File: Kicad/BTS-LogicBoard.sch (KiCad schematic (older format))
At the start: 39 parts, among them J1 Conn_01x06, J2 Conn_01x04, J3 Conn_01x02, SW1 SW_DPDT_x2, SW2 SW_DPDT_x2, U1 NCS2252SN2T1G, U2 NE555D, U3 74HC1GU04, U4 TLP291, U5 74HC1GU04, U6 NCS2252SN2T1G

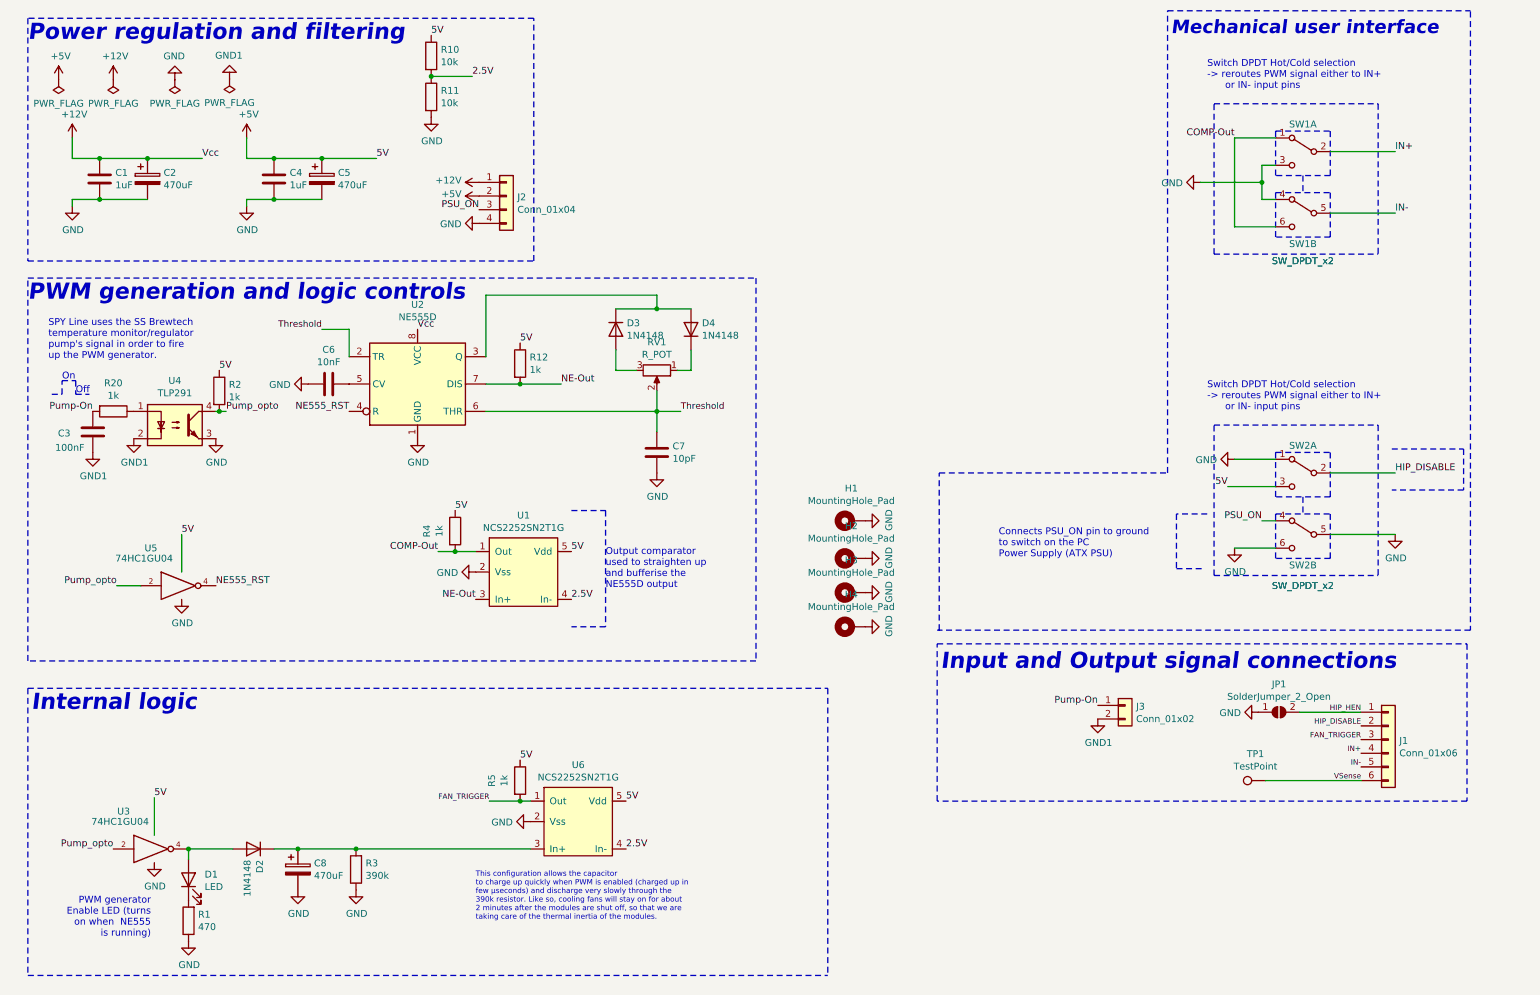
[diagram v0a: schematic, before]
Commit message: Updated schematic with LEDS and new NE555/TS555 PWM generation circuit
Signed-off-by: bebenlebricolo <benoittarrade@hotmail.fr>
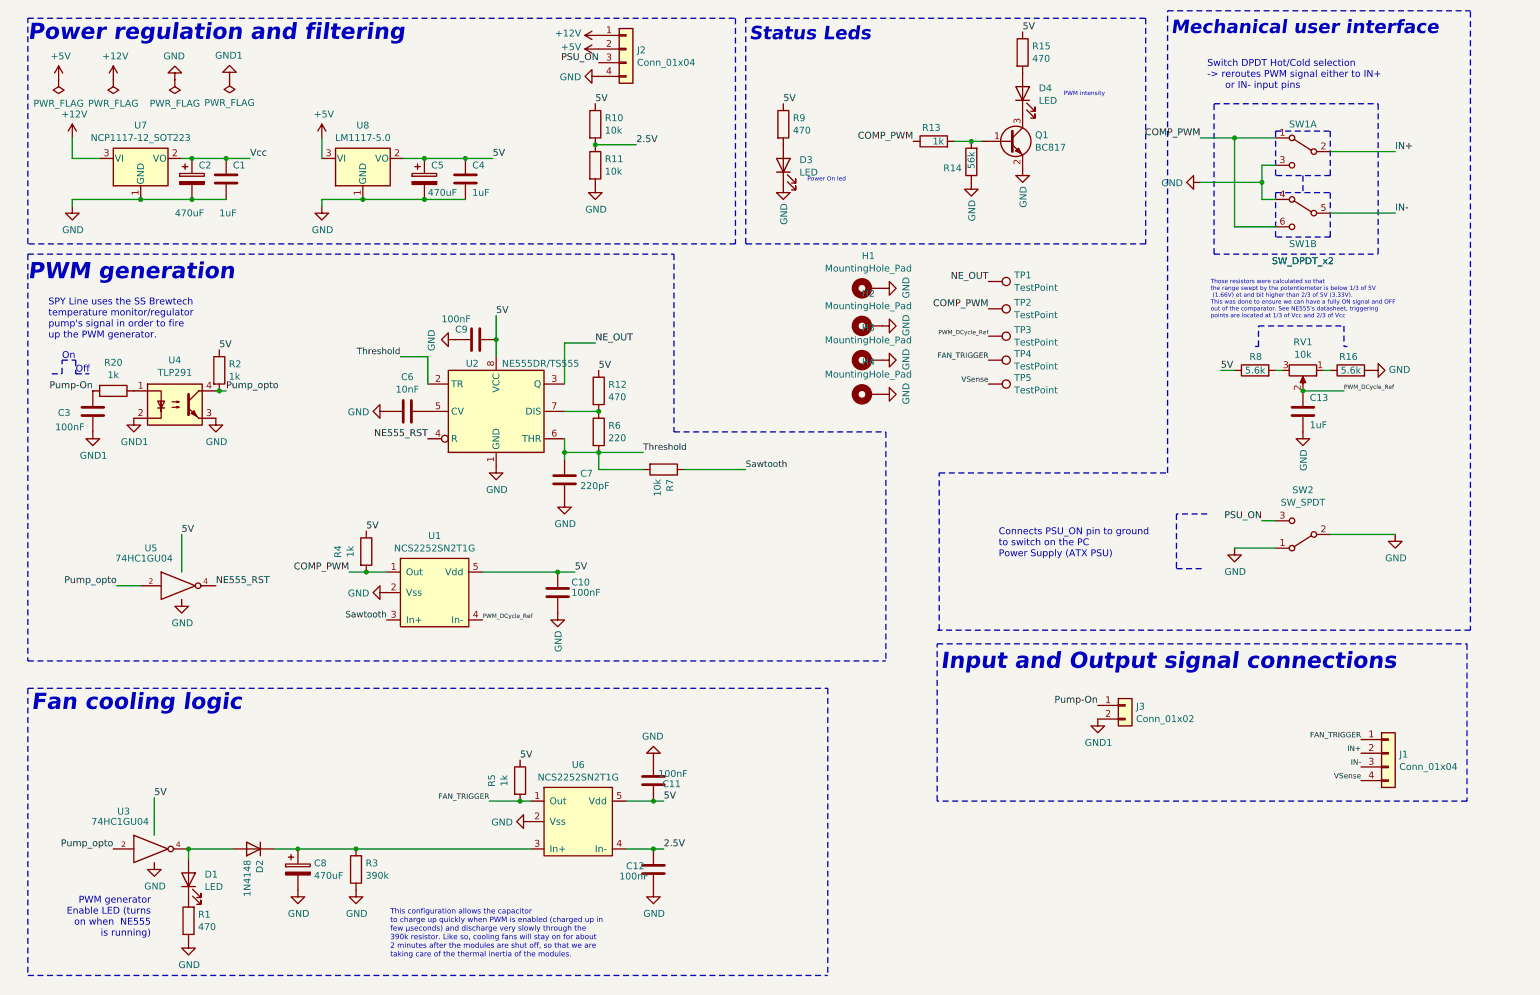
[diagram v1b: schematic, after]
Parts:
- removed D3, D4: 1N4148, Diode_SMD:D_1206_3216Metric_Pad1.42x1.75mm_HandSolder, symbol Diode:1N4148
- removed J1: Conn_01x06, BTS-LogicBoard:Molex_MicroLock_1.25_01x06, symbol Connector_Generic:Conn_01x06
- removed JP1: SolderJumper_2_Open, Jumper:SolderJumper-2_P1.3mm_Open_RoundedPad1.0x1.5mm, symbol Jumper:SolderJumper_2_Open
- removed SW2: SW_DPDT_x2, BTS-LogicBoard:PinSocket_2x03_P2.54mm_Vertical_DPDT_Special, symbol Switch:SW_DPDT_x2
- added C10, C11, C12, C9: 100nF, Capacitor_SMD:C_1206_3216Metric_Pad1.33x1.80mm_HandSolder, symbol Device:C
- added C13: 1uF, Capacitor_SMD:C_1206_3216Metric_Pad1.33x1.80mm_HandSolder, symbol Device:C
- added D3, D4: LED, symbol Device:LED
- added J1: Conn_01x04, BTS-LogicBoard:TE_EP_01x04_2132230-4, symbol Connector_Generic:Conn_01x04
- added Q1: BC817, Package_TO_SOT_SMD:SOT-23, symbol Transistor_BJT:BC817
- added R13: 1k, Resistor_SMD:R_1206_3216Metric_Pad1.30x1.75mm_HandSolder, symbol Device:R
- added R14: 56k, Resistor_SMD:R_1206_3216Metric_Pad1.30x1.75mm_HandSolder, symbol Device:R
- added R15, R9: 470, Resistor_SMD:R_1206_3216Metric_Pad1.30x1.75mm_HandSolder, symbol Device:R
- added R16, R8: 5.6k, Resistor_SMD:R_1206_3216Metric_Pad1.30x1.75mm_HandSolder, symbol Device:R
- added R6: 220, Resistor_SMD:R_1206_3216Metric_Pad1.30x1.75mm_HandSolder, symbol Device:R
- added R7: 10k, Resistor_SMD:R_1206_3216Metric_Pad1.30x1.75mm_HandSolder, symbol Device:R
- added SW2: SW_SPDT, symbol Switch:SW_SPDT
- added TP2, TP3, TP4, TP5: TestPoint, symbol Connector:TestPoint
- added U7: NCP1117-12_SOT223, Package_TO_SOT_SMD:SOT-223-3_TabPin2, symbol Regulator_Linear:NCP1117-12_SOT223
- added U8: LM1117-5.0, symbol Regulator_Linear:LM1117-5.0
- C7: value 10pF -> 220pF; Link (none) -> https://fr.rs-online.com/web/p/condensateurs-ceramique-mult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; Model (none) -> 1206Y1K00221KXT
- R12: value 1k -> 470
- RV1: value R_POT -> 10k; footprint Connector_PinSocket_2.54mm:PinSocket_1x03_P2.54mm_Vertical -> (none)
- TP1: footprint TestPoint:TestPoint_Pad_D2.0mm -> (none)
- U2: value NE555D -> NE555DR/TS555
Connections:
- net +12V: now also U7.3 (VI); no longer C1.1, C2.1, U2.8 (VCC)
- net +5V: now also U8.3 (VI); no longer C4.1, C5.1, R10.1, R12.1, R2.1, R4.1, R5.1, U1.5 (Vdd), U3.5 (VCC), U5.5 (VCC), U6.5 (Vdd)
- net 2.5V: now also C12.1; no longer U1.4 (In-)
- net FAN_TRIGGER: now also J1.1 (Pin_1), TP4.1
- net GND: now also C10.2, C11.2, C12.2, C13.2, C9.2, D3.1 (K), Q1.2 (E), R14.1, R16.2, SW2.1 (A), SW2.2 (B), U7.1 (GND), U8.1 (GND)
- net IN+: now also J1.2 (Pin_2)
- net IN-: now also J1.3 (Pin_3)
- net PSU_ON: now also SW2.3 (C)
- net Threshold: now also R6.2, R7.2; no longer RV1.2
- net VSense: now also J1.4 (Pin_4), TP5.1; no longer TP1.1
- net NE_OUT: now reaches U2.3 (Q)
- net NE_OUT: now also TP1.1
- net at RV1.3: now also R8.2
- net at RV1.1: now also R16.1
- net COMP-Out renamed COMP_PWM
- net COMP_PWM: now also R13.1, TP2.1
- net NE-Out: no longer names the net of R12.2, U2.7 (DIS)
- net NE-Out: now also R6.1; no longer U1.3 (In+)
- new net: D3.2 (A), R9.2
- new net: D4.2 (A), R15.2
- new net: D4.1 (K), Q1.3 (C)
- new net: Q1.1 (B), R13.2, R14.2
- new net PWM_DCycle_Ref: C13.1, RV1.2, TP3.1, U1.4 (In-)
- new net Sawtooth: R7.1, U1.3 (In+)
- new net VCC: C10.1, C11.1, C4.1, C5.1, C9.1, R10.1, R12.1, R15.1, R2.1, R4.1, R5.1, R8.1, R9.1, U1.5 (Vdd), U2.8 (VCC), U3.5 (VCC), U5.5 (VCC), U6.5 (Vdd), U8.2 (VO)
- new net Vcc: C1.1, C2.1, U7.2 (VO)
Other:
- note added: "Fan cooling logic"
- note added: "PWM generation"
- note added: "PWM intensity"
- note added: "Power On led"
- note added: "Status Leds"
- note added: "Those resistors were calculated so that\nthe range swept by the potentiometer is below 1/3 of 5V\n (1.66V) et and bit higher than 2/3 of 5V (3.33V).\nThis was done to ensure we can have a fully ON signal and OFF\nout of the comparator. See NE555's datasheet, triggering\npoints are located at 1/3 of Vcc and 2/3 of Vcc"
- note removed: "Internal logic"
- note removed: "Output comparator \nused to straighten up \nand bufferise the \nNE555D output"
- note removed: "PWM generation and logic controls"
- moved on the sheet: C1, C2, C3, C4, C5, C6, C7, H1, H2, H3, H4, J2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

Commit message: Restarted layout
Signed-off-by: bebenlebricolo <benoittarrade@hotmail.fr>
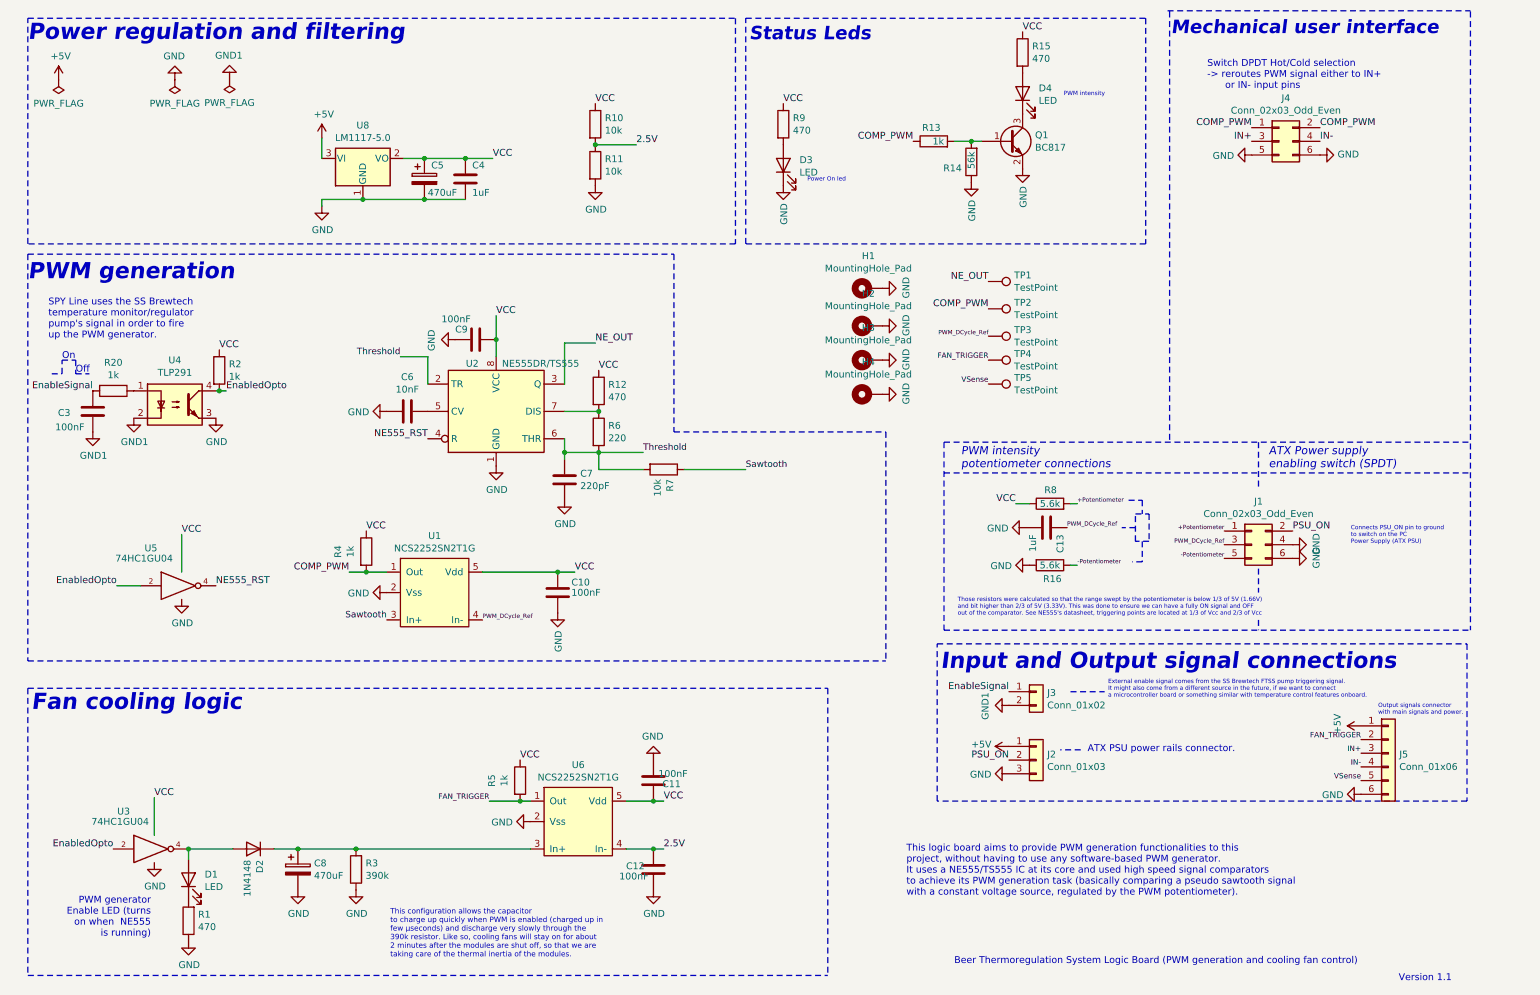
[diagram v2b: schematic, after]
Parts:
- removed C1: 1uF, Capacitor_SMD:C_1206_3216Metric_Pad1.33x1.80mm_HandSolder, symbol Device:C
- removed C2: 470uF, Capacitor_SMD:CP_Elec_10x10, symbol Device:CP
- removed J1: Conn_01x04, BTS-LogicBoard:TE_EP_01x04_2132230-4, symbol Connector_Generic:Conn_01x04
- removed J2: Conn_01x04, Connector_PinSocket_2.54mm:PinSocket_1x04_P2.54mm_Vertical, symbol Connector_Generic:Conn_01x04
- removed RV1: 10k, symbol Device:R_POT
- removed SW1: SW_DPDT_x2, BTS-LogicBoard:PinSocket_2x03_P2.54mm_Vertical_DPDT_Special, symbol Switch:SW_DPDT_x2
- removed SW2: SW_SPDT, symbol Switch:SW_SPDT
- removed U7: NCP1117-12_SOT223, Package_TO_SOT_SMD:SOT-223-3_TabPin2, symbol Regulator_Linear:NCP1117-12_SOT223
- added J1, J4: Conn_02x03_Odd_Even, Connector_Hirose:Hirose_DF11-6DP-2DSA_2x03_P2.00mm_Vertical, symbol Connector_Generic:Conn_02x03_Odd_Even
- added J2: Conn_01x03, BTS-LogicBoard:559350310, symbol Connector_Generic:Conn_01x03
- added J5: Conn_01x06, BTS-LogicBoard:Molex_MicroLock_1.25_01x06, symbol Connector_Generic:Conn_01x06
- D3, D4: footprint (none) -> LED_THT:LED_D3.0mm
- TP1, TP2, TP3, TP4, TP5: footprint (none) -> TestPoint:TestPoint_Pad_D2.0mm
- U8: footprint (none) -> Package_TO_SOT_SMD:SOT-223-3_TabPin2
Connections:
- net +5V: now also J2.1 (Pin_1), J5.1 (Pin_1)
- net COMP_PWM: now also J4.1 (Pin_1), J4.2 (Pin_2)
- net FAN_TRIGGER: now also J5.2 (Pin_2)
- net GND: now also J1.4 (Pin_4), J1.6 (Pin_6), J2.3 (Pin_3), J4.5 (Pin_5), J4.6 (Pin_6), J5.6 (Pin_6)
- net IN+: now also J4.3 (Pin_3), J5.3 (Pin_3)
- net IN-: now also J4.4 (Pin_4), J5.4 (Pin_4)
- net PSU_ON: now also J1.2 (Pin_2), J2.2 (Pin_2)
- net PWM_DCycle_Ref: now also J1.3 (Pin_3)
- net VSense: now also J5.5 (Pin_5)
- net -Potentiometer: now reaches R16.1
- net -Potentiometer: now also J1.5 (Pin_5)
- net +Potentiometer: now reaches R8.2
- net +Potentiometer: now also J1.1 (Pin_1)
- net Pump-On renamed EnableSignal
- net Pump_opto renamed EnabledOpto
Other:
- note added: "ATX PSU power rails connector."
- note added: "ATX Power supply\nenabling switch (SPDT)"
- note added: "Beer Thermoregulation System Logic Board (PWM generation and cooling fan control)"
- note added: "External enable signal comes from the SS Brewtech FTSS pump triggering signal.\nIt might also come from a different source in the future, if we want to connect\na microcontroller board or something similar with temperature control features onboard."
- note added: "Output signals connector \nwith main signals and power."
- note added: "PWM intensity \npotentiometer connections"
- note added: "This logic board aims to provide PWM generation functionalities to this\nproject, without having to use any software-based PWM generator.\nIt uses a NE555/TS555 IC at its core and used high speed signal comparators\nto achieve its PWM generation task (basically comparing a pseudo sawtooth signal\nwith a constant voltage source, regulated by the PWM potentiometer)."
- note added: "Those resistors were calculated so that the range swept by the potentiometer is below 1/3 of 5V (1.66V) \nand bit higher than 2/3 of 5V (3.33V). This was done to ensure we can have a fully ON signal and OFF\nout of the comparator. See NE555's datasheet, triggering points are located at 1/3 of Vcc and 2/3 of Vcc"
- note added: "Version 1.1"
- note removed: "Those resistors were calculated so that\nthe range swept by the potentiometer is below 1/3 of 5V\n (1.66V) et and bit higher than 2/3 of 5V (3.33V).\nThis was done to ensure we can have a fully ON signal and OFF\nout of the comparator. See NE555's datasheet, triggering\npoints are located at 1/3 of Vcc and 2/3 of Vcc"
- moved on the sheet: C13, J3, R16, R8

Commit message: Finalized layout for Version 1.1 (need to work on silkscreen now)
Signed-off-by: bebenlebricolo <benoittarrade@hotmail.fr>
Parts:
- U3: footprint Package_TO_SOT_SMD:SOT-353_SC-70-5_Handsoldering -> Package_TO_SOT_SMD:SOT-353_SC-70-5
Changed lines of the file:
@@
 F 0 "U3" H 1325 6925 50  0000 C CNN
 F 1 "74HC1GU04" H 1300 6850 50  0000 C CNN
-F 2 "Package_TO_SOT_SMD:SOT-353_SC-70-5_Handsoldering" H 1550 6650 50  0001 C CNN
+F 2 "Package_TO_SOT_SMD:SOT-353_SC-70-5" H 1550 6650 50  0001 C CNN
 F 3 "https://assets.nexperia.com/documents/data-sheet/74HC1GU04.pdf" H 1550 6650 50  0001 C CNN
 	1    1550 6650
